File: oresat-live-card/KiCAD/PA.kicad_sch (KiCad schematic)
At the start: 33 parts, among them J5 2X1_TH_JUMPER, J9 Conn_Coaxial, U17 PAT1220-C-3DB, U19 TQP9111, U6 SN74LVC1G32QDBVRQ1, U8 MIC94090YC6-TR

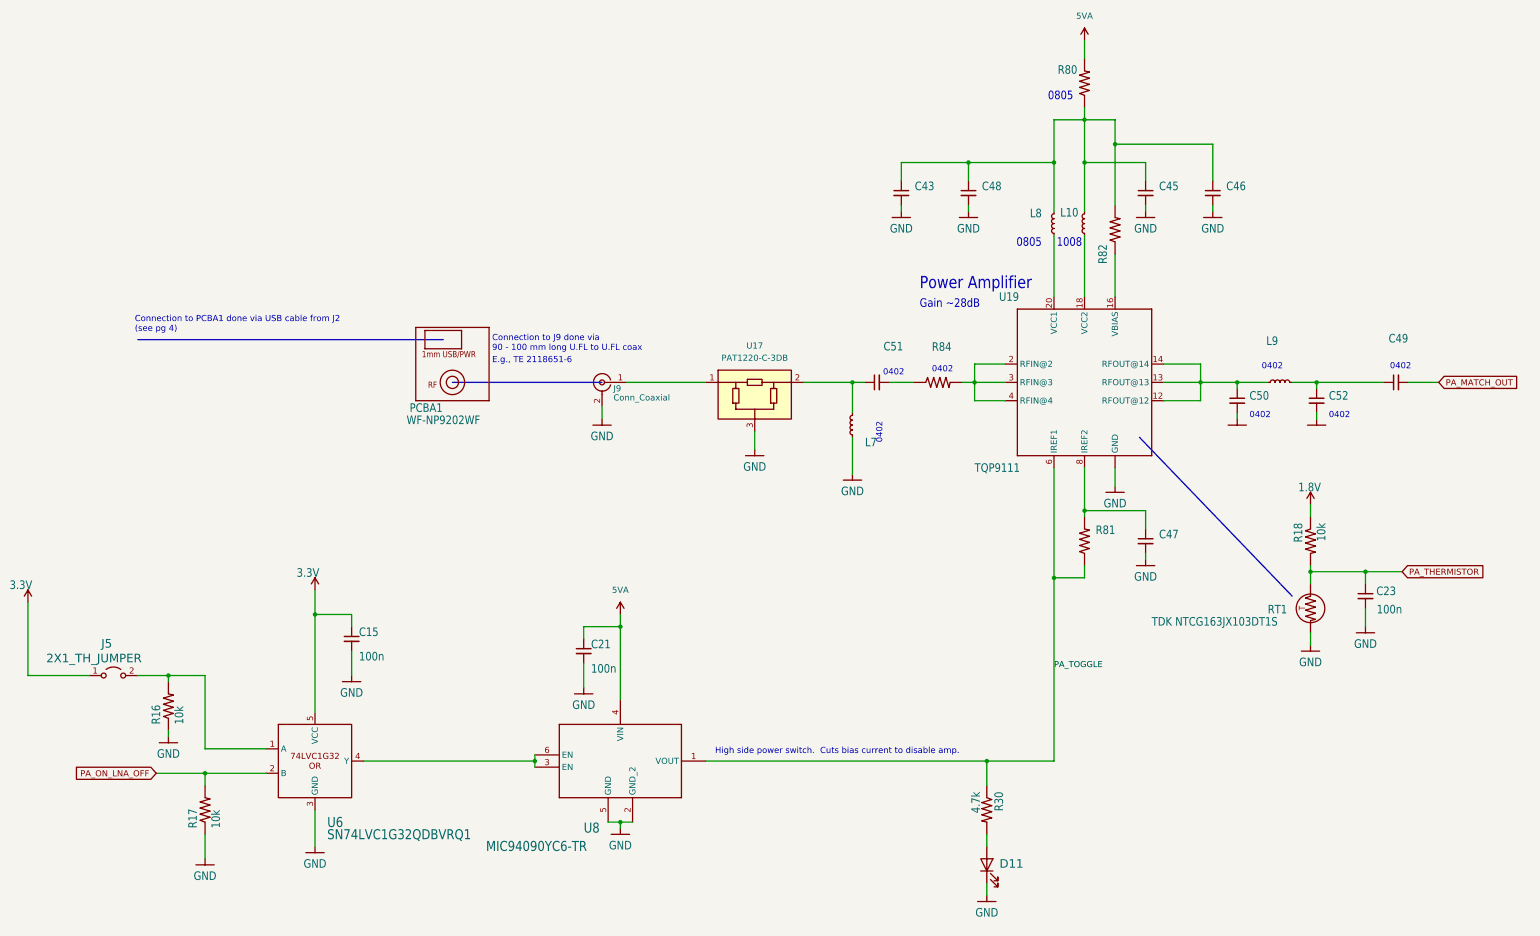
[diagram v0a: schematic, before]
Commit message: completed tx/rx switch circuit and cleaned up GND references
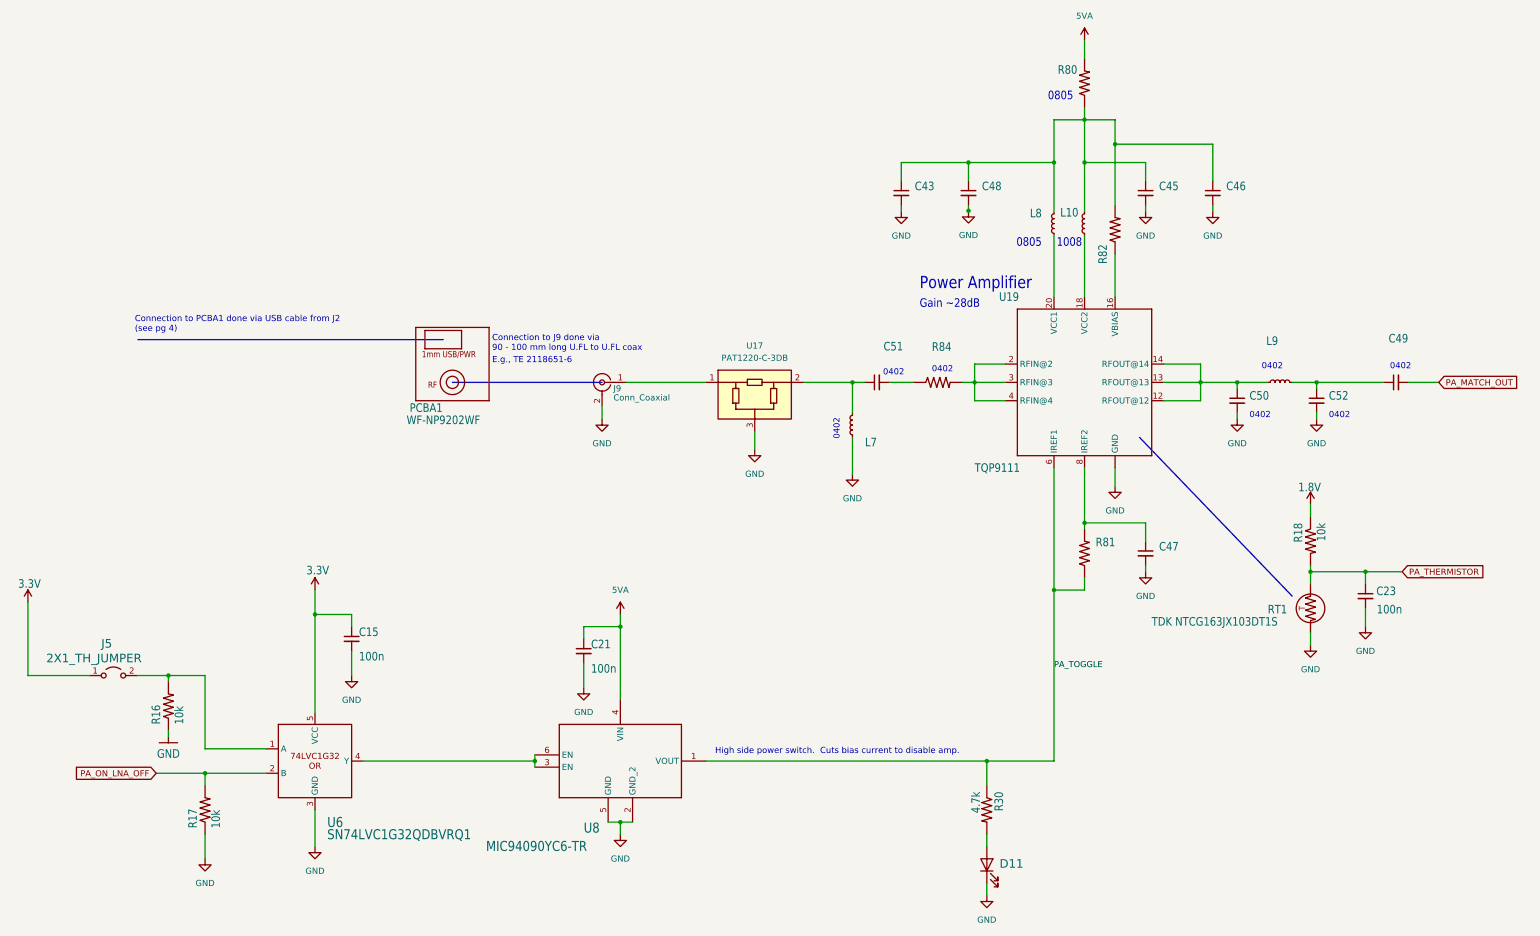
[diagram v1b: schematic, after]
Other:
- moved on the sheet: C47, R81

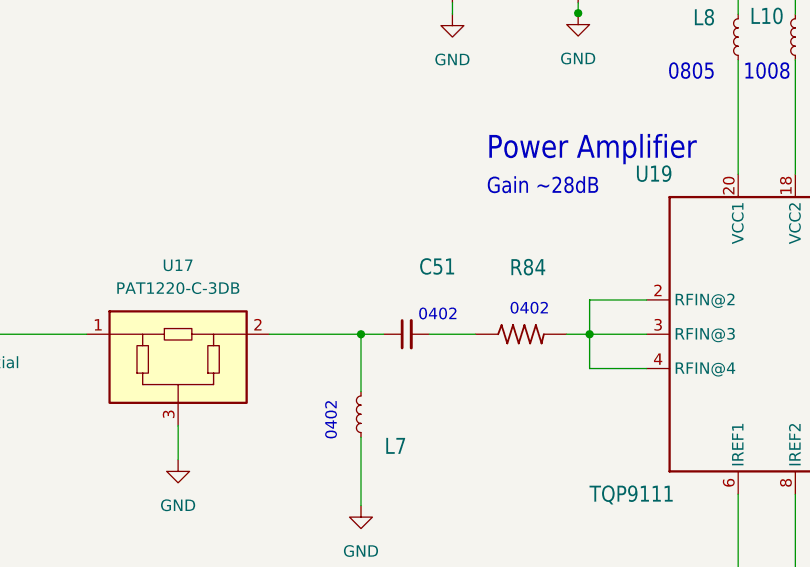
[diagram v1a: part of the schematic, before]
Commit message: completed LNA minus pwr detect.
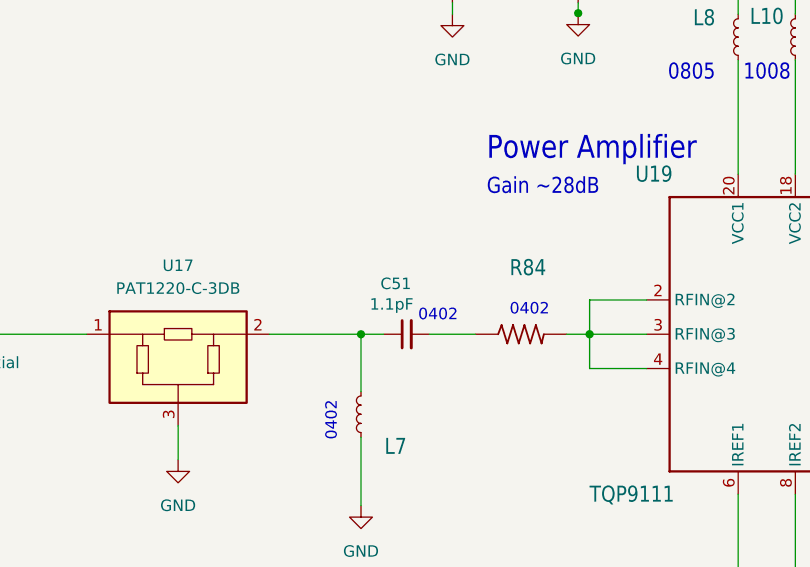
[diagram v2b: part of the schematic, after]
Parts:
- C51: value 04025J1R1PBSTR\500 -> 1.1pF
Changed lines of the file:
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@@
 		(dnp no)
 		(property "Reference" "C51"
-			(at 216.281 105.791 90)
+			(at 211.328 107.95 90)
 			(effects
 				(font
-					(size 1.778 1.5113)
+					(size 1.27 1.27)
 				)
 				(justify left bottom)
 			)
 		)
-		(property "Value" "04025J1R1PBSTR\\500"
-			(at 210.82 114.3 0)
+		(property "Value" "1.1pF"
+			(at 211.582 110.236 90)
 			(effects
 				(font
-					(size 1.778 1.5113)
+					(size 1.27 1.27)
 				)
 				(justify left bottom)
-				(hide yes)
 			)
 		)

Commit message: implemented notes from Oliver. Added notes for self to fix later
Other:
- note added: "UPDATE TO 1.4"
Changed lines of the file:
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@@
 	(title_block
 		(title "Oresat DxWifi Card")
-		(date "2024-01-02")
+		(date "2025-05-28")
 		(rev "2")
 	)
@@
 		)
 	)
+	(text "UPDATE TO 1.4\n"
+		(exclude_from_sim no)
+		(at 214.122 117.856 0)
+		(effects
+			(font
+				(size 1.27 1.27)
+			)
+		)
+	)

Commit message: implemented notes form Oliver J
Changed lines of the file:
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@@
 		(rev "2")
 	)
+	(text "Connection to PCBA1 done via USB cable from J2\n(see pg 4)\n\n"
+		(exclude_from_sim no)
+		(at 56.515 106.045 0)
+		(effects
+			(font
+				(size 1.27 1.27)
+			)
+			(justify left bottom)
+		)
+	)
 	(text "0402\n"
 		(exclude_from_sim no)
@@
 		)
 	)
+	(text "E.g., TE 2118651-6"
+		(exclude_from_sim no)
+		(at 130.81 110.49 0)
+		(effects
+			(font
+				(size 1.27 1.27)
+			)
+			(justify left bottom)
+		)
+	)
 	(text "0402\n"
 		(exclude_from_sim no)
@@
 		)
 	)
-	(text "Gain ~28dB"
+	(text "Connection to J9 done via \n90 - 100 mm long U.FL to U.FL coax\n"
 		(exclude_from_sim no)
-		(at 219.71 99.06 0)
+		(at 130.81 107.95 0)
 		(effects
 			(font
-				(size 1.778 1.5113)
+				(size 1.27 1.27)
 			)
 			(justify left bottom)
 		)
 	)
-	(text "0805"
+	(text "Gain ~28dB"
 		(exclude_from_sim no)
-		(at 246.38 55.88 0)
+		(at 219.71 99.06 0)
 		(effects
 			(font
@@
 		)
 	)
-	(text "E.g., TE 2118651-6"
+	(text "0805"
 		(exclude_from_sim no)
-		(at 130.81 110.49 0)
+		(at 246.38 55.88 0)
 		(effects
 			(font
-				(size 1.27 1.27)
+				(size 1.778 1.5113)
 			)
 			(justify left bottom)
@@
 		)
 	)
-	(text "Connection to PCBA1 done via USB cable from J2\n(see pg 4)\n\n"
-		(exclude_from_sim no)
-		(at 56.515 106.045 0)
-		(effects
-			(font
-				(size 1.27 1.27)
-			)
-			(justify left bottom)
-		)
-	)
 	(text "UPDATE TO 1.4\n"
 		(exclude_from_sim no)
@@
 		)
 	)
-	(text "Connection to J9 done via \n90 - 100 mm long U.FL to U.FL coax\n"
-		(exclude_from_sim no)
-		(at 130.81 107.95 0)
-		(effects
-			(font
-				(size 1.27 1.27)
-			)
-			(justify left bottom)
-		)
-	)
 	(junction
 		(at 71.12 195.58)
@@
 		)
 	)
+	(polyline
+		(pts
+			(xy 57.15 105.41) (xy 119.38 105.41)
+		)
+		(stroke
+			(width 0)
+			(type default)
+		)
+	)
 	(wire
 		(pts
@@
 		)
 	)
-	(polyline
+	(wire
 		(pts
-			(xy 57.15 105.41) (xy 120.65 105.41)
+			(xy 280.67 77.47) (xy 280.67 78.74)
 		)
 		(stroke
@@
 	(wire
 		(pts
-			(xy 280.67 77.47) (xy 280.67 78.74)
+			(xy 215.9 72.39) (xy 215.9 68.58)
 		)
 		(stroke
@@
 		)
 	)
-	(wire
+	(polyline
 		(pts
-			(xy 215.9 72.39) (xy 215.9 68.58)
+			(xy 121.92 114.3) (xy 153.67 114.3)
 		)
 		(stroke
@@
 		)
 	)
-	(polyline
-		(pts
-			(xy 122.555 114.3) (xy 153.67 114.3)
-		)
-		(stroke
-			(width 0)
-			(type default)
-		)
-	)
 	(wire
 		(pts
@@
 	(symbol
 		(lib_id "oresat-live-card-eagle-import:WF-NP9202WF")
-		(at 122.555 110.49 0)
+		(at 121.92 110.49 0)
 		(unit 1)
 		(exclude_from_sim no)
@@
 		(dnp no)
 		(property "Reference" "PCBA1"
-			(at 113.665 120.65 0)
+			(at 113.03 120.65 0)
 			(effects
 				(font
@@
 				)
 				(justify left bottom)
+				(hide yes)
 			)
 		)
 		(property "Value" "WF-NP9202WF"
-			(at 113.03 123.19 0)
+			(at 114.3 120.65 0)
 			(effects
 				(font
-					(size 1.778 1.5113)
+					(size 1.27 1.27)
 				)
 				(justify left bottom)
@@
 		)
 		(property "Footprint" "oresat-live-card:WF-NP9202"
-			(at 122.555 110.49 0)
+			(at 121.92 110.49 0)
 			(effects
 				(font
@@
 		)
 		(property "Datasheet" ""
-			(at 122.555 110.49 0)
+			(at 121.92 110.49 0)
 			(effects
 				(font
@@
 		)
 		(property "Description" ""
-			(at 122.555 110.49 0)
+			(at 121.92 110.49 0)
 			(effects
 				(font

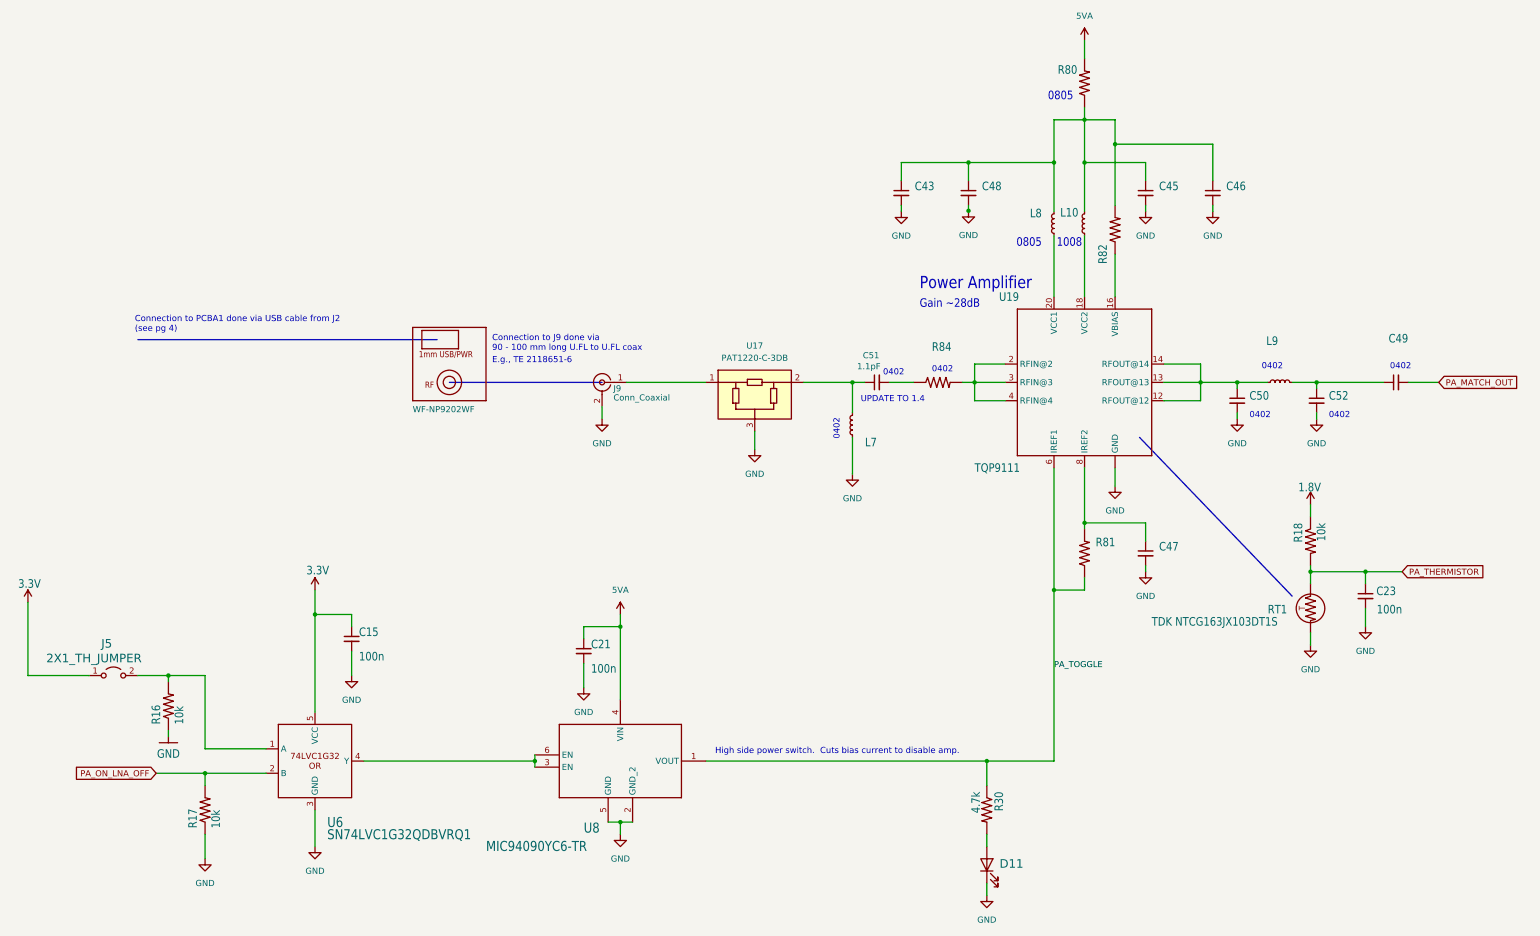
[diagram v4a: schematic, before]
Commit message: Fixed up schematic as best as possible. There were a lot of issues with local paths being referenced, and EAGLE import libraries. Fixed all of those, as well as fixed some oresat-kicad IC symbols (bad direction pins) and I think we're now OK. Also updated card outline for two RF (LEFT) connectors.  Still missing two packages, but we'll deal with that later.
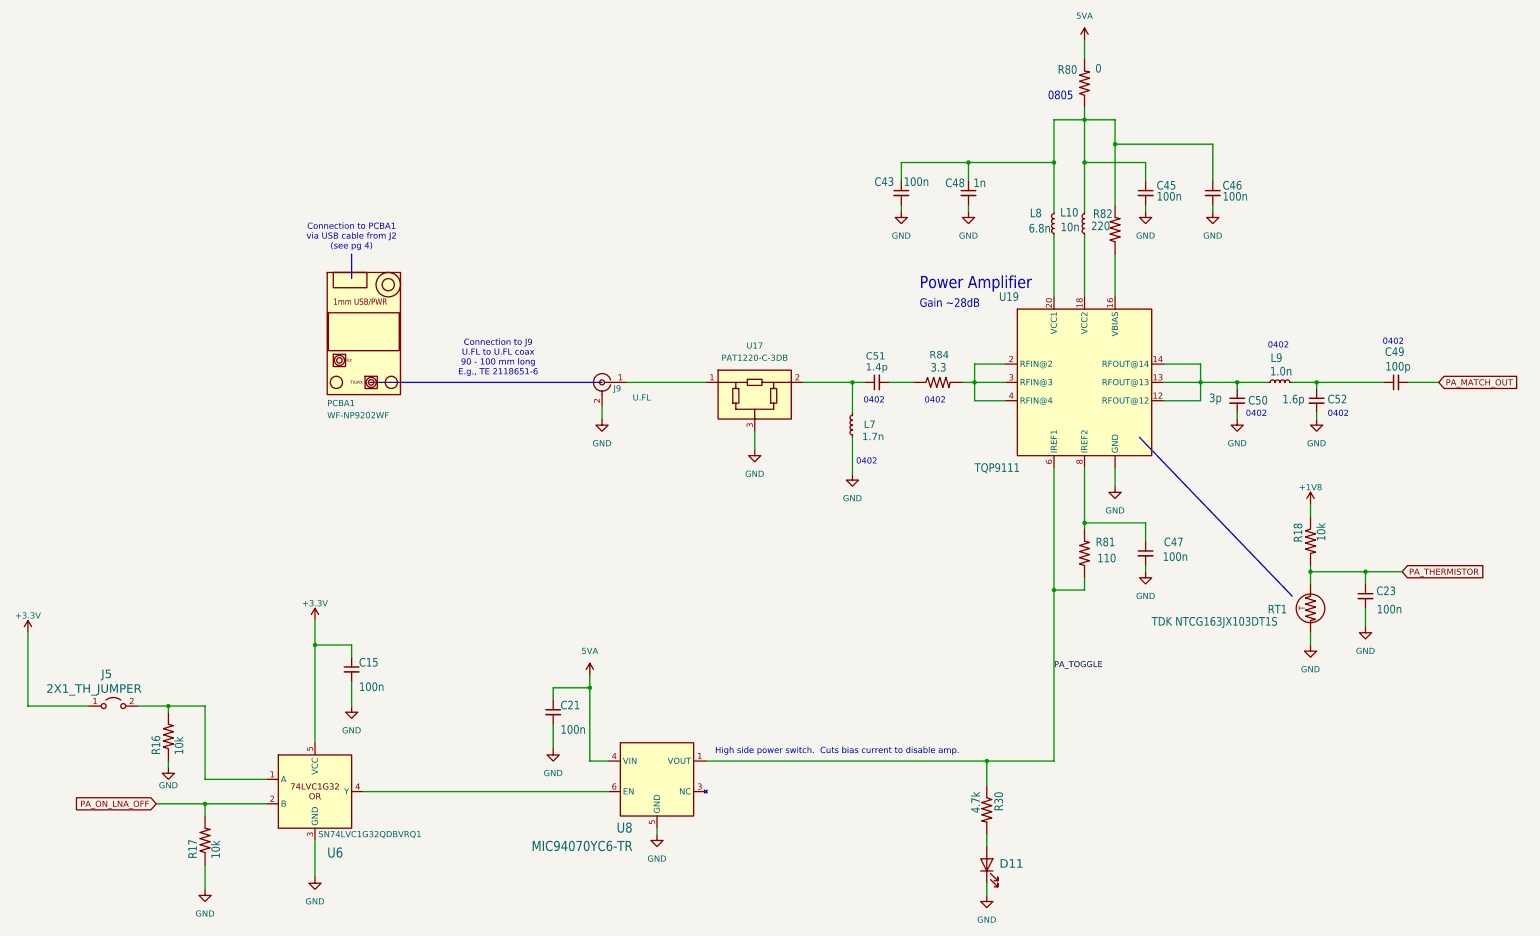
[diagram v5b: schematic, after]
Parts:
- C15, C21, C23: DPN (none) -> 445-5667-1-ND; MFR (none) -> TDK Corporation; MPN CL10B104KB8WPNC -> CGA3E2X7R1E104K080AA
- C43, C45, C46, C47: value CGA2B1X7R1C104K050BC -> 100n; DPN (none) -> 445-5667-1-ND; MFR (none) -> TDK Corporation; MPN CL10B104KB8WPNC -> CGA3E2X7R1E104K080AA
- C48: value CGA2B2NP01H102J050BA -> 1n; DPN (none) -> 445-12118-1-ND; MFR (none) -> TDK Corporation; MPN TMF105B7102KVHF -> CGA2B2NP01H102J050BA
- C49: value GCM1885C1H101JA16D -> 100p; DPN (none) -> 490-GCM1555C1H101GA16DCT-ND; MFR (none) -> Murata Electronics; MPN C0402C101K4RACAUTO -> GCM1555C1H101GA16D
- C50: value 04025U3R0BAT2A -> 3p; DPN (none) -> 581-04025U3R0BAT2A; Distributor DigiKey -> Mouser; MFR (none) -> KYOCERA AVX; MPN 04025U3R0BAT2A -> 04025U3R0BAT2A
- C51: value 1.1pF -> 1.4p; DPN (none) -> 581-04025J1R4PBSTR5; Distributor DigiKey -> Mouser; MFR (none) -> KYOCERA AVX
- C52: value 04025U1R6BAT2A -> 1.6p; DPN (none) -> 581-04025U1R6BAT2A; Distributor DigiKey -> Mouser; MFR (none) -> KYOCERA AVX; MPN 04025U1R6BAT2A -> 04025U1R6BAT2A
- D11: value 150060VS55040 -> GREEN; DPN (none) -> 732-150060GS75020CT-ND; MFR (none) -> Würth Elektronik
- J9: value Conn_Coaxial -> U.FL; DPN (none) -> H11891CT-ND; Distributor (none) -> DigiKey; MFR (none) -> Hirose Electric Co Ltd; MPN (none) -> U.FL-R-SMT-1(10)
- L10: value Fixed Inductors 1008 10nH Unshld 5% 1.6A 60mOhms -> 10n; DPN (none) -> 1008HQ-10NXJLC; Distributor DigiKey -> Coilcraft; MFR (none) -> Coilcraft; MPN 1008HQ-10NXJLB -> 1008HQ-10NXJLC
- L7: value 0402DC-1N7XJRU -> 1.7n; DPN (none) -> 994-0402DC-1N7XJRW; Distributor DigiKey -> Mouser; MFR (none) -> Coilcraft
- L8: value 0805CS-060XJLC -> 6.8n.; DPN (none) -> 994-0805CS-060XJLC; Distributor DigiKey -> Mouser; MFR (none) -> Coilcraft
- L9: value MLK1005S1N0ST000 -> 1.0n; DPN (none) -> 445-MLK1005S1N0ST000CT-ND; MFR (none) -> TDK Corporation
- PCBA1: symbol oresat-live-card-eagle-import:WF-NP9202WF -> oresat-pcbs:WF-NP9202WF
- R16, R17, R18: DPN (none) -> P10.0KHCT-ND; MFR (none) -> Panasonic
- R30: DPN (none) -> ERJ-3EKF4701V; MFR (none) -> Panasonic; MPN ERJ-3EKF1002V -> ERJ-3EKF4701V
- R80: value ERJ-6GEY0R00V -> 0; DPN (none) -> P0.0ACT-ND; MFR (none) -> Panasonic
- R81: value ERJ-2RKF1100X -> 110; DPN (none) -> P110LCT-ND; MFR (none) -> Panasonic
- R82: value ERJ-3EKF2200V -> 220; DPN (none) -> P220HCT-ND; MFR (none) -> Panasonic
- R84: value CRCW04023R30FKED -> 3.3; DPN (none) -> 541-3.30LLCT-ND; MFR (none) -> Vishay Dale
- RT1: DPN (none) -> 445-174518-1-ND; MFR (none) -> TDK Corporation
- U17: DPN (none) -> PAT123CT-ND; Distributor (none) -> DigiKey; MFR (none) -> Susumu; MPN (none) -> PAT1220-C-3DB-T5
- U19: DPN (none) -> 2312-TQP9111CT-ND; MFR (none) -> Qorvo
- U6: footprint oresat-live-card:DBV5 -> (none); Distributor DigiKey -> (none); MPN SN74LVC1G32QDBVRQ1 -> (none)
- U8: value MIC94090YC6-TR -> MIC94070YC6-TR; DPN (none) -> 576-3006-1-ND; MFR (none) -> Microchip Technology; MPN MIC94090YC6 -> MIC94070YC6-TR
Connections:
- net at U6.4 (Y), U8.6 (EN): no longer U8.3 (EN)
- net 1.8V renamed +1V8
- net 3.3V renamed +3.3V
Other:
- note added: "Connection to J9 U.FL to U.FL coax 90 - 100 mm long E.g., TE 2118651-6"
- note added: "Connection to PCBA1 via USB cable from J2 (see pg 4)"
- note removed: "1008"
- note removed: "Connection to J9 done via 90 - 100 mm long U.FL to U.FL coax"
- note removed: "Connection to PCBA1 done via USB cable from J2 (see pg 4)"
- note removed: "E.g., TE 2118651-6"
- note removed: "UPDATE TO 1.4"
- moved on the sheet: C15, C21, J5, R16, R17
